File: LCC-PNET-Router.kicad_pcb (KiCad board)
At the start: 2 copper layers, 63.5 x 119.4 mm, 45 parts, among them J101 USB_A, J201 Termination, J202 RJ45, J203 RJ45, J301 Termination, J302 PNET, J303 PNET, P1 POCKETBEAGLE-P1, P2 POCKETBEAGLE-P2, T201 LCC Power Out, T202 LCC Power In, U201 LM358, U202 TCAN332DR, U301 LM358, U302 TCAN332DR, U401 AP63205

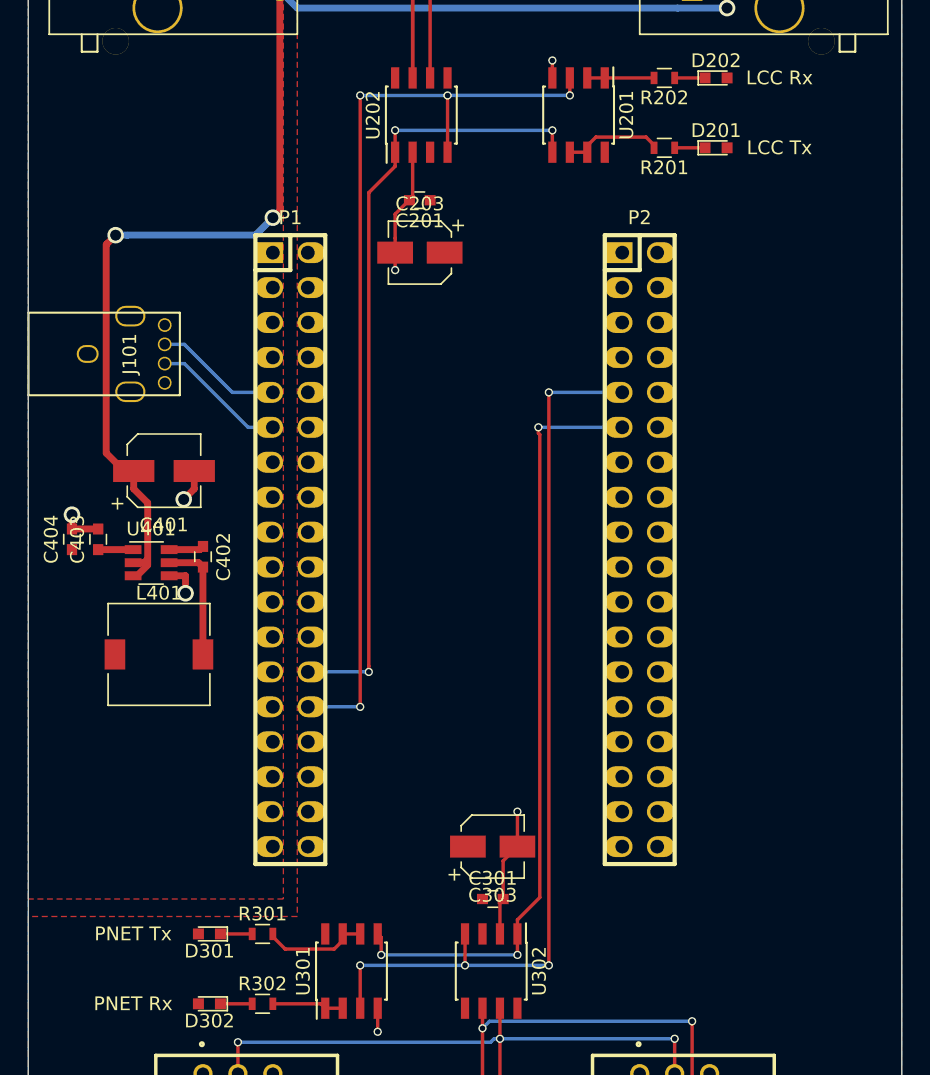
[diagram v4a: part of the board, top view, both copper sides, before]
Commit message: Complete 3D and final touches on PCB.
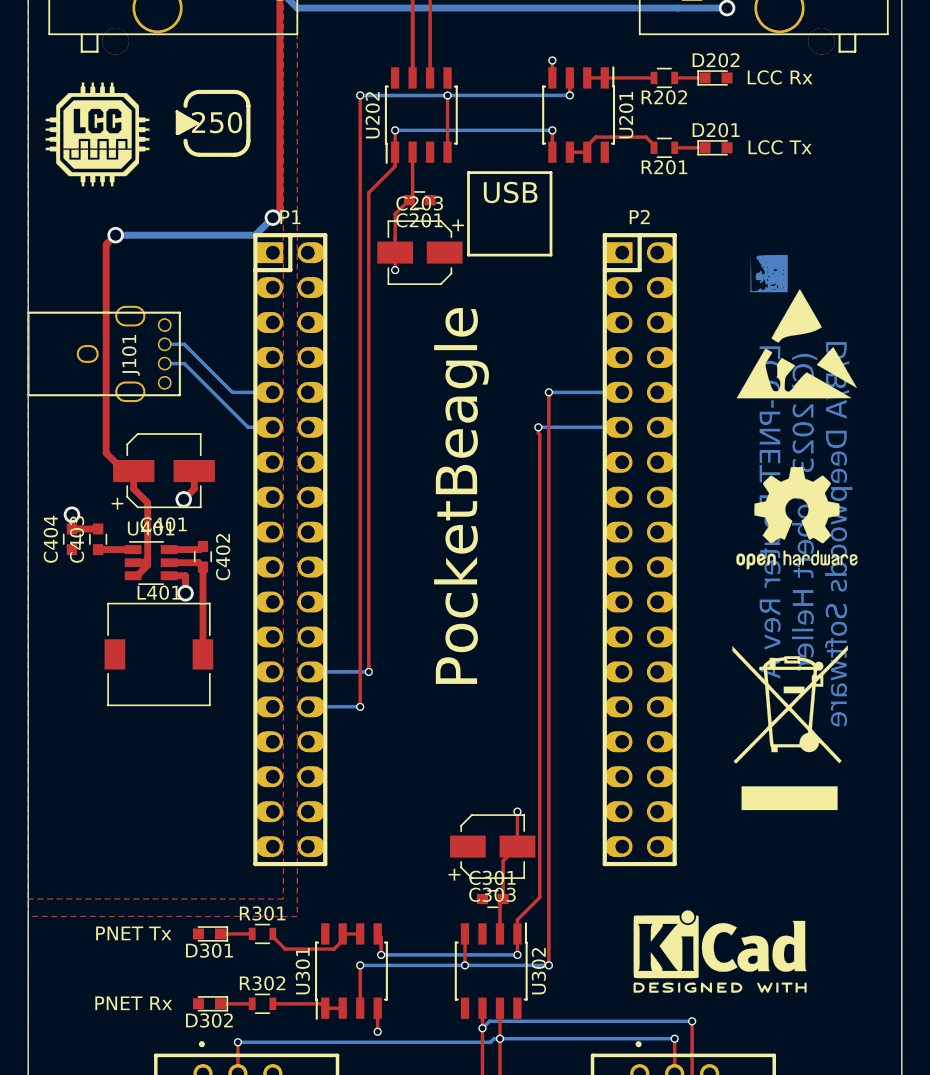
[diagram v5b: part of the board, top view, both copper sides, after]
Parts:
- added ?: , DWSLogoBCU:DWSLogoBCU, F.Cu at (163.1, 82.8)
- added G***: LCC, LCC_LOGO:LCC_LOGO_9x9, F.Cu at (114.3, 72.6)
- added REF**: PowerLabel-250, PowerLabels:PowerLabel-250, F.Cu at (122.9, 71.9)
- added REF***: ESD-Logo_8.9x8mm_SilkScreen, Symbols:ESD-Logo_8.9x8mm_SilkScreen, F.Cu at (165.1, 87.9)
- added REF***: KiCad-Logo2_6mm_SilkScreen, Symbols:KiCad-Logo2_6mm_SilkScreen, F.Cu at (159.5, 132.1)
- added REF***: OSHW-Logo2_9.8x8mm_SilkScreen, Symbols:OSHW-Logo2_9.8x8mm_SilkScreen, F.Cu at (165.1, 100.6)
- added REF***: WEEE-Logo_8.4x12mm_SilkScreen, Symbols:WEEE-Logo_8.4x12mm_SilkScreen, F.Cu at (164.6, 115.8)
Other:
- board text added: "LCC-PNET-Router Rev A (C) 2023 Robert Heller D/B/A Deepwoods Software"
- board text added: "PocketBeagle"
- board text added: "USB"

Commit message: Last minute update: dims and fids.
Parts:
- added REF**: Fiducial_classic_Small_SilkscreenTop_Type1, Fiducials:Fiducial_classic_Small_SilkscreenTop_Type1, F.Cu at (118.1, 121.9)
- added REF**: Fiducial_classic_Small_SilkscreenTop_Type1, Fiducials:Fiducial_classic_Small_SilkscreenTop_Type1, F.Cu at (141.0, 57.1)
- added REF**: Fiducial_classic_Small_SilkscreenTop_Type1, Fiducials:Fiducial_classic_Small_SilkscreenTop_Type1, F.Cu at (165.1, 129.5)
- moved REF*** 25.3 mm to (138.4, 118.1)
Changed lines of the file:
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@@
     (links 111)
     (no_connects 0)
-    (area 109.169999 38.049999 172.770001 157.530001)
+    (area 96.845716 25.24 191.444286 158.945)
     (thickness 1.6)
-    (drawings 11)
+    (drawings 17)
     (tracks 251)
     (zones 0)
-    (modules 52)
+    (modules 55)
     (nets 101)
   )
@@
   )
   (module Symbols:KiCad-Logo2_6mm_SilkScreen (layer F.Cu)
-    (at 159.512 132.08)
+    (at 138.43 118.11)
     (descr "KiCad Logo")
     (tags "Logo KiCad")
@@
       (xy 4.208431 -5.985209) (xy 4.207205 -5.812752)) (layer F.SilkS) (width 0.01))
   )
+  (module Fiducials:Fiducial_classic_Small_SilkscreenTop_Type1 (layer F.Cu)
+    (at 118.11 121.92)
+    (descr "Fiducial, Classical, Small, Copper Top, Typ 1, Passermarke,")
+    (tags "Fiducial, Classical, Small, Copper Top, Typ 1, Passermarke,")
+    (fp_text reference REF** (at 0 -3.556) (layer F.SilkS) hide
+      (effects (font (size 1 1) (thickness 0.15)))
+    )
+    (fp_text value Fiducial_classic_Small_SilkscreenTop_Type1 (at 0.34036 3.4798) (layer F.Fab) hide
+      (effects (font (size 1 1) (thickness 0.15)))
+    )
+    (fp_line (start -1.50114 0) (end 1.50114 0) (layer F.SilkS) (width 0.15))
+    (fp_line (start 0 -1.50114) (end 0 1.50114) (layer F.SilkS) (width 0.15))
+    (fp_circle (center 0 0) (end 1.50114 0) (layer F.SilkS) (width 0.15))
+    (pad ~ smd circle (at 0 0) (size 4.50088 4.50088) (layers F.Mask)
+      (solder_mask_margin 2.99974))
+  )
+  (module Fiducials:Fiducial_classic_Small_SilkscreenTop_Type1 (layer F.Cu)
+    (at 140.97 57.15)
+    (descr "Fiducial, Classical, Small, Copper Top, Typ 1, Passermarke,")
+    (tags "Fiducial, Classical, Small, Copper Top, Typ 1, Passermarke,")
+    (fp_text reference REF** (at 0 -3.556) (layer F.SilkS) hide
+      (effects (font (size 1 1) (thickness 0.15)))
+    )
+    (fp_text value Fiducial_classic_Small_SilkscreenTop_Type1 (at 0.34036 3.4798) (layer F.Fab) hide
+      (effects (font (size 1 1) (thickness 0.15)))
+    )
+    (fp_line (start -1.50114 0) (end 1.50114 0) (layer F.SilkS) (width 0.15))
+    (fp_line (start 0 -1.50114) (end 0 1.50114) (layer F.SilkS) (width 0.15))
+    (fp_circle (center 0 0) (end 1.50114 0) (layer F.SilkS) (width 0.15))
+    (pad ~ smd circle (at 0 0) (size 4.50088 4.50088) (layers F.Mask)
+      (solder_mask_margin 2.99974))
+  )
+  (module Fiducials:Fiducial_classic_Small_SilkscreenTop_Type1 (layer F.Cu)
+    (at 165.1 129.54)
+    (descr "Fiducial, Classical, Small, Copper Top, Typ 1, Passermarke,")
+    (tags "Fiducial, Classical, Small, Copper Top, Typ 1, Passermarke,")
+    (fp_text reference REF** (at 0 -3.556) (layer F.SilkS) hide
+      (effects (font (size 1 1) (thickness 0.15)))
+    )
+    (fp_text value Fiducial_classic_Small_SilkscreenTop_Type1 (at 0.34036 3.4798) (layer F.Fab) hide
+      (effects (font (size 1 1) (thickness 0.15)))
+    )
+    (fp_line (start -1.50114 0) (end 1.50114 0) (layer F.SilkS) (width 0.15))
+    (fp_line (start 0 -1.50114) (end 0 1.50114) (layer F.SilkS) (width 0.15))
+    (fp_circle (center 0 0) (end 1.50114 0) (layer F.SilkS) (width 0.15))
+    (pad ~ smd circle (at 0 0) (size 4.50088 4.50088) (layers F.Mask)
+      (solder_mask_margin 2.99974))
+  )
+  (dimension 111.76 (width 0.3) (layer Dwgs.User)
+    (gr_text "111.760 mm" (at 104.06 97.79 270) (layer Dwgs.User)
+      (effects (font (size 1.5 1.5) (thickness 0.3)))
+    )
+    (feature1 (pts (xy 113.03 153.67) (xy 102.71 153.67)))
+    (feature2 (pts (xy 113.03 41.91) (xy 102.71 41.91)))
+    (crossbar (pts (xy 105.41 41.91) (xy 105.41 153.67)))
+    (arrow1a (pts (xy 105.41 153.67) (xy 104.823579 152.543496)))
+    (arrow1b (pts (xy 105.41 153.67) (xy 105.996421 152.543496)))
+    (arrow2a (pts (xy 105.41 41.91) (xy 104.823579 43.036504)))
+    (arrow2b (pts (xy 105.41 41.91) (xy 105.996421 43.036504)))
+  )
+  (dimension 55.88 (width 0.3) (layer Dwgs.User)
+    (gr_text "55.880 mm" (at 140.97 34.21) (layer Dwgs.User)
+      (effects (font (size 1.5 1.5) (thickness 0.3)))
+    )
+    (feature1 (pts (xy 168.91 41.91) (xy 168.91 32.86)))
+    (feature2 (pts (xy 113.03 41.91) (xy 113.03 32.86)))
+    (crossbar (pts (xy 113.03 35.56) (xy 168.91 35.56)))
+    (arrow1a (pts (xy 168.91 35.56) (xy 167.783496 36.146421)))
+    (arrow1b (pts (xy 168.91 35.56) (xy 167.783496 34.973579)))
+    (arrow2a (pts (xy 113.03 35.56) (xy 114.156504 36.146421)))
+    (arrow2b (pts (xy 113.03 35.56) (xy 114.156504 34.973579)))
+  )
+  (dimension 3.81 (width 0.3) (layer Dwgs.User)
+    (gr_text "3.810 mm" (at 105.33 40.005 90) (layer Dwgs.User)
+      (effects (font (size 1.5 1.5) (thickness 0.3)))
+    )
+    (feature1 (pts (xy 113.03 38.1) (xy 103.98 38.1)))
+    (feature2 (pts (xy 113.03 41.91) (xy 103.98 41.91)))
+    (crossbar (pts (xy 106.68 41.91) (xy 106.68 38.1)))
+    (arrow1a (pts (xy 106.68 38.1) (xy 107.266421 39.226504)))
+    (arrow1b (pts (xy 106.68 38.1) (xy 106.093579 39.226504)))
+    (arrow2a (pts (xy 106.68 41.91) (xy 107.266421 40.783496)))
+    (arrow2b (pts (xy 106.68 41.91) (xy 106.093579 40.783496)))
+  )
+  (dimension 3.81 (width 0.3) (layer Dwgs.User)
+    (gr_text "3.810 mm" (at 111.125 34.21) (layer Dwgs.User)
+      (effects (font (size 1.5 1.5) (thickness 0.3)))
+    )
+    (feature1 (pts (xy 109.22 41.91) (xy 109.22 32.86)))
+    (feature2 (pts (xy 113.03 41.91) (xy 113.03 32.86)))
+    (crossbar (pts (xy 113.03 35.56) (xy 109.22 35.56)))
+    (arrow1a (pts (xy 109.22 35.56) (xy 110.346504 34.973579)))
+    (arrow1b (pts (xy 109.22 35.56) (xy 110.346504 36.146421)))
+    (arrow2a (pts (xy 113.03 35.56) (xy 111.903496 34.973579)))
+    (arrow2b (pts (xy 113.03 35.56) (xy 111.903496 36.146421)))
+  )
+  (dimension 119.38 (width 0.3) (layer Dwgs.User)
+    (gr_text "119.380 mm" (at 184.23 97.79 270) (layer Dwgs.User)
+      (effects (font (size 1.5 1.5) (thickness 0.3)))
+    )
+    (feature1 (pts (xy 172.72 157.48) (xy 185.58 157.48)))
+    (feature2 (pts (xy 172.72 38.1) (xy 185.58 38.1)))
+    (crossbar (pts (xy 182.88 38.1) (xy 182.88 157.48)))
+    (arrow1a (pts (xy 182.88 157.48) (xy 182.293579 156.353496)))
+    (arrow1b (pts (xy 182.88 157.48) (xy 183.466421 156.353496)))
+    (arrow2a (pts (xy 182.88 38.1) (xy 182.293579 39.226504)))
+    (arrow2b (pts (xy 182.88 38.1) (xy 183.466421 39.226504)))
+  )
+  (dimension 63.5 (width 0.3) (layer Dwgs.User)
+    (gr_text "63.500 mm" (at 140.97 26.59) (layer Dwgs.User)
+      (effects (font (size 1.5 1.5) (thickness 0.3)))
+    )
+    (feature1 (pts (xy 172.72 38.1) (xy 172.72 25.24)))
+    (feature2 (pts (xy 109.22 38.1) (xy 109.22 25.24)))
+    (crossbar (pts (xy 109.22 27.94) (xy 172.72 27.94)))
+    (arrow1a (pts (xy 172.72 27.94) (xy 171.593496 28.526421)))
+    (arrow1b (pts (xy 172.72 27.94) (xy 171.593496 27.353579)))
+    (arrow2a (pts (xy 109.22 27.94) (xy 110.346504 28.526421)))
+    (arrow2b (pts (xy 109.22 27.94) (xy 110.346504 27.353579)))
+  )
   (gr_text "PocketBeagle\n" (at 140.462 99.06 90) (layer F.SilkS)

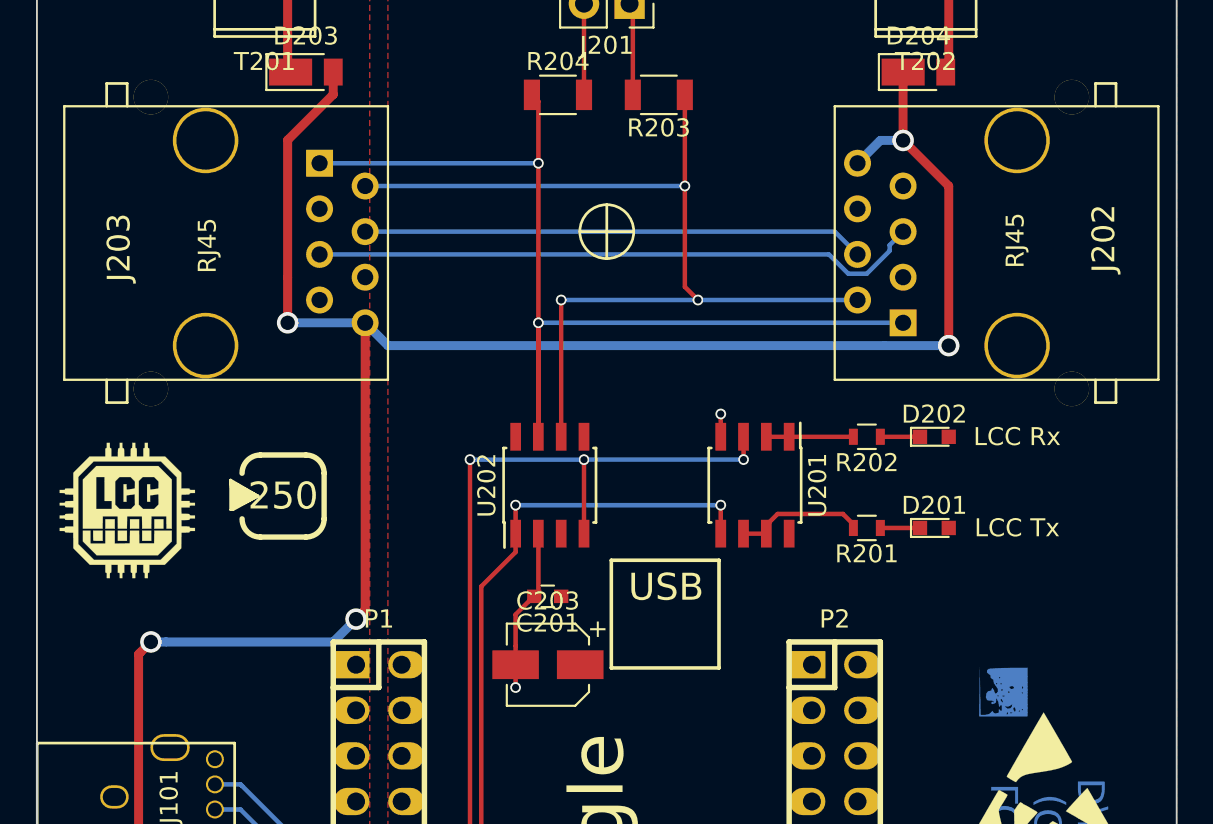
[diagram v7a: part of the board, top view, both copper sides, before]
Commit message: Update PCB: fix errors.
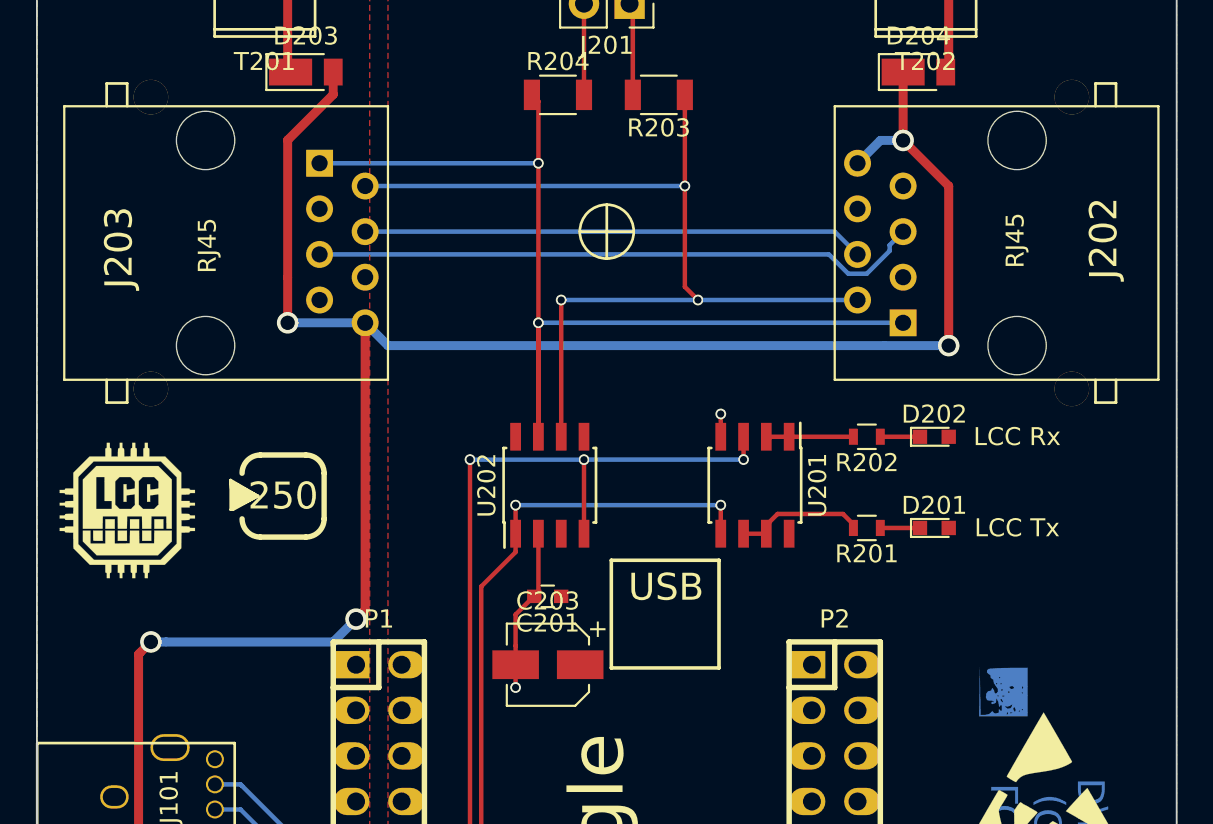
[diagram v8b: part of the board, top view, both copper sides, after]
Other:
- net class Default removed
